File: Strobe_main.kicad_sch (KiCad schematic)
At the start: 0 parts

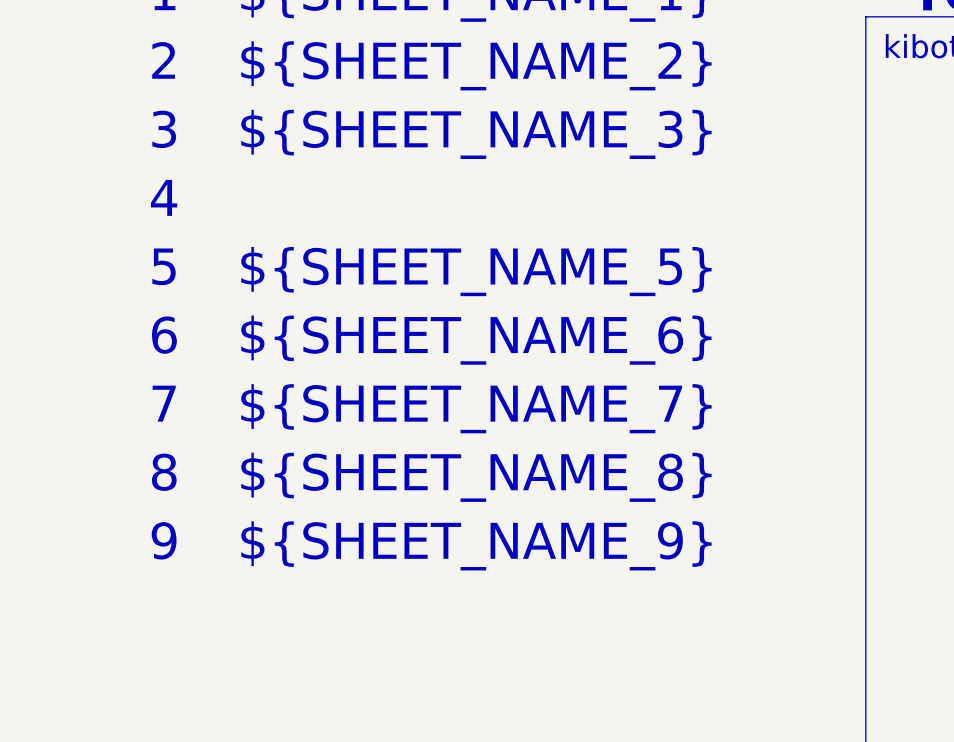
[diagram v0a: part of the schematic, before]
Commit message: Fixed small DFM warnings from JLCPCB
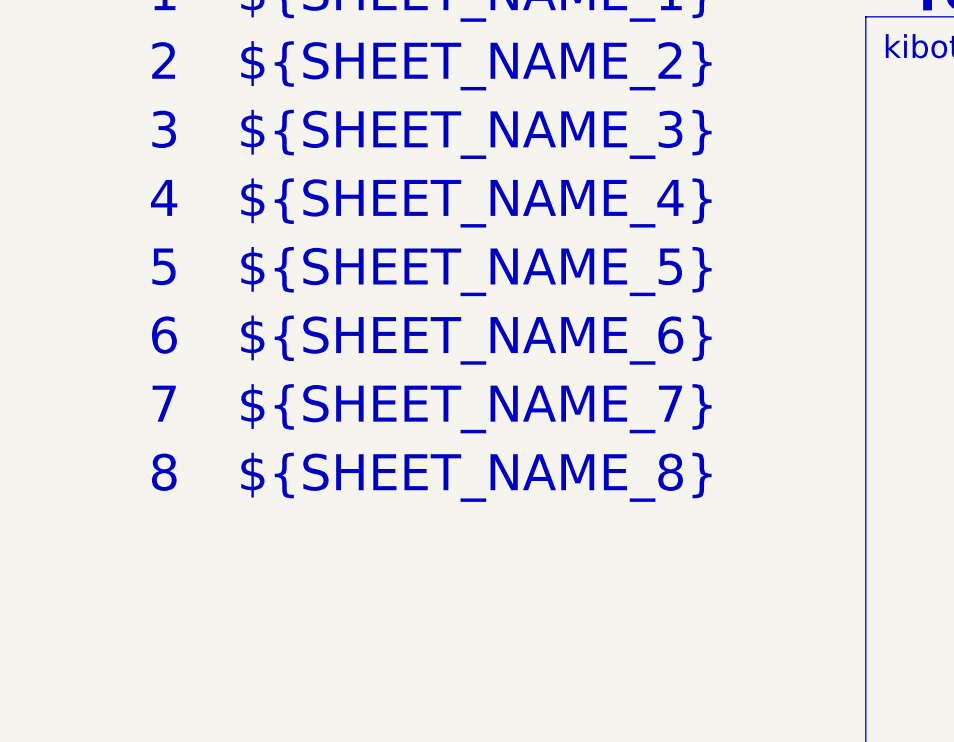
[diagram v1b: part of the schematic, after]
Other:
- note added: "${SHEET_NAME_4}"
- note removed: "${SHEET_NAME_9}"
- note removed: "9"
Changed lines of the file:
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@@
 		)
 	)
-	(text "${SHEET_NAME_9}"
+	(text "${SHEET_NAME_4}"
 		(exclude_from_sim no)
-		(at 38.1 124.46 0)
+		(at 38.1 86.36 0)
 		(effects
 			(font
@@
 		)
 	)
-	(text "9"
-		(exclude_from_sim no)
-		(at 31.75 124.46 0)
-		(effects
-			(font
-				(face "Times New Roman")
-				(size 4 4)
-				(color 0 0 0 1)
-			)
-			(justify right bottom)
-			(href "#9")
-		)
-	)
